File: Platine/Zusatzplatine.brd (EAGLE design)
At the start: 70 x 62.2 mm, 23 parts

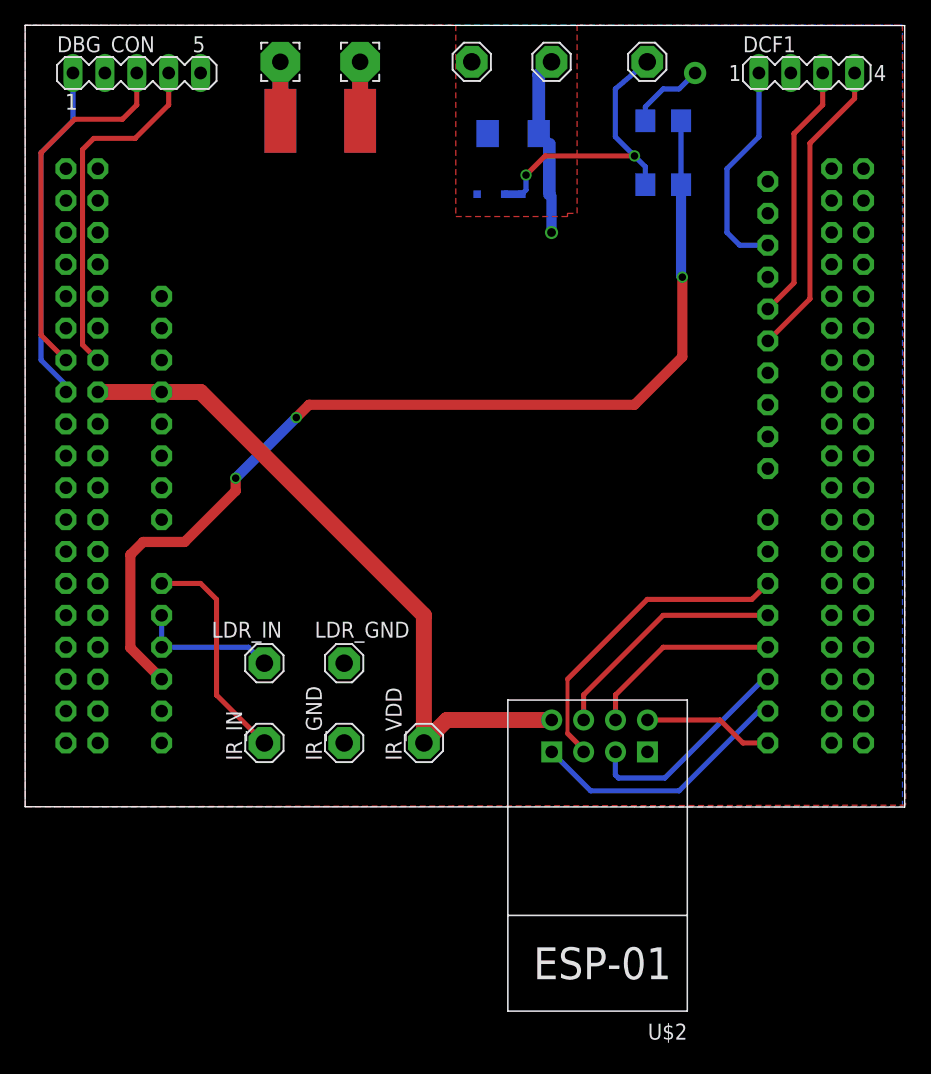
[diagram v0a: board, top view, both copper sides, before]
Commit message: Added Upside Down Mount Option for WiFI Improved Documentation on Board
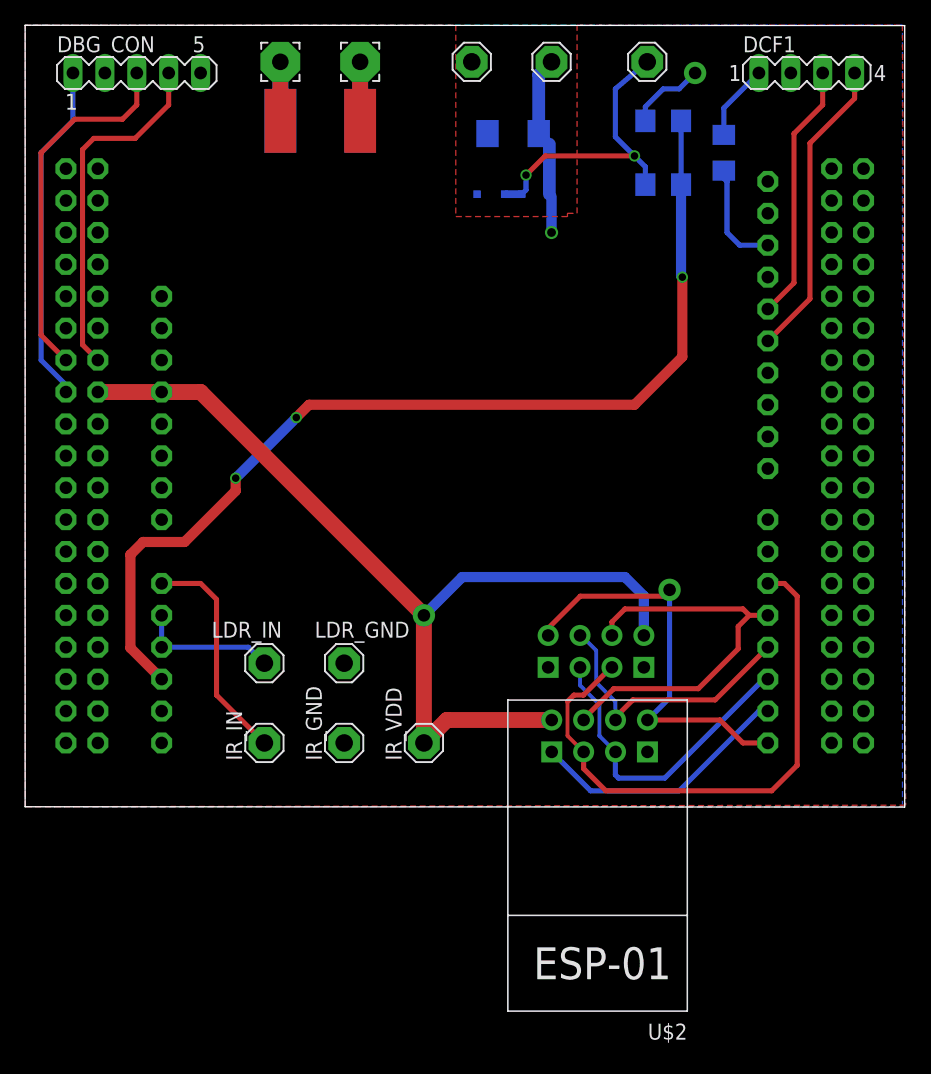
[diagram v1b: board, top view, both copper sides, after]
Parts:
- added R3: 120R, rcl:R1206
- added U$3: ESP01, esp8266modules:ESP01
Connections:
- new net N$2: DCF1.1, R3.1
- net +3V3: now also U$3.VCC
- net GND: now also U$3.GND
- net N$1: now also R3.2; no longer DCF1.1
- net N$12: now also U$3.GPIO0
- net N$13: now also U$3.RST
- net N$14: now also U$3.CH_PD
- net N$15: now also U$3.TX
- net N$16: now also U$3.RX
- net N$17: now also U$3.GPIO2
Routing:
- net N$15: track 10.3 -> 32.9 mm, vias 0 -> 1
- net +3V3: track 54.4 -> 77.0 mm, vias 0 -> 1
- net N$12: track 25.4 -> 45.3 mm
- net N$13: track 19.3 -> 31.9 mm
- net N$17: track 17.3 -> 25.2 mm
- net N$1: track 17.4 -> 9.72 mm
- net N$14: track 15.7 -> 22.6 mm
- net N$2: track 0.00 -> 6.09 mm
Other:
- board text added: "CLK"
- board text added: "DATA"
- board text added: "GND"
- board text added: "NRST"
- board text added: "PON"
- board text added: "SWDIO"
- board text added: "VCC"
- board text added: "WiFi BOT MNT"
- board text added: "WiFi TOP MNT"

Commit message: - DCF-Leitungen umgelegt - Doku korrigiert
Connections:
- net DCF1_DATA: now also U$1.SCL; no longer U$1.D13
- net DCF1_PON: now also U$1.SDA; no longer U$1.D12
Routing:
- net N$16: track 21.1 -> 32.4 mm
- net DCF1_PON: track 24.2 -> 14.0 mm
- net DCF1_DATA: track 20.6 -> 10.4 mm
- net N$14: vias 0 -> 1
- net N$13: vias 0 -> 2
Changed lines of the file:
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@@
 <?xml version="1.0" encoding="utf-8"?>
 <!DOCTYPE eagle SYSTEM "eagle.dtd">
-<eagle version="7.2.0">
+<eagle version="7.4.0">
 <drawing>
 <settings>
@@
 <wire x1="70.028" y1="62.19579375" x2="0" y2="62.22" width="0" layer="20"/>
 <wire x1="0" y1="62.22" x2="0" y2="0" width="0" layer="20"/>
-<text x="19.05" y="33.02" size="1.778" layer="51">WC-WS-Shield for Nucleo
+<text x="19.05" y="33.02" size="1.778" layer="25">WC-WS-Shield for Nucleo
 (c) 2015 K. Neumann, J. Berg</text>
 <text x="33.528" y="53.721" size="1.27" layer="51" rot="R90">LED GND</text>
@@
 <text x="64.008" y="52.832" size="1.016" layer="51" rot="R90">DATA</text>
 <text x="62.992" y="52.705" size="1.016" layer="52" rot="MR90">DATA</text>
-<text x="52.324" y="33.274" size="1.778" layer="52" rot="MR0">WC-WS-Shield for Nucleo
+<text x="52.324" y="33.274" size="1.778" layer="26" rot="MR0">WC-WS-Shield for Nucleo
 (c) 2015 K. Neumann, J. Berg</text>
 </plain>
@@
 <wire x1="44.465" y1="7" x2="46.863" y2="9.398" width="0.4064" layer="1"/>
 <wire x1="46.863" y1="9.398" x2="53.594" y2="9.398" width="0.4064" layer="1"/>
-<wire x1="53.594" y1="9.398" x2="56.769" y2="12.573" width="0.4064" layer="1"/>
-<wire x1="56.769" y1="12.573" x2="56.769" y2="14.351" width="0.4064" layer="1"/>
+<wire x1="53.594" y1="9.398" x2="56.769" y2="12.573" width="0.4064" layer="16"/>
+<wire x1="56.769" y1="12.573" x2="56.769" y2="14.351" width="0.4064" layer="16"/>
 <wire x1="56.769" y1="14.351" x2="57.658" y2="15.24" width="0.4064" layer="1"/>
 <wire x1="57.658" y1="15.24" x2="59.13" y2="15.24" width="0.4064" layer="1"/>
@@
 <wire x1="47.752" y1="15.748" x2="57.15" y2="15.748" width="0.4064" layer="1"/>
 <wire x1="57.15" y1="15.748" x2="57.658" y2="15.24" width="0.4064" layer="1"/>
+<via x="53.594" y="9.398" extent="1-16" drill="0.6" shape="square"/>
+<via x="56.769" y="14.351" extent="1-16" drill="0.6" shape="square"/>
 </signal>
 <signal name="N$14">
@@
 <wire x1="47.005" y1="7.127" x2="48.387" y2="8.509" width="0.4064" layer="1"/>
 <wire x1="48.387" y1="8.509" x2="54.939" y2="8.509" width="0.4064" layer="1"/>
-<wire x1="54.939" y1="8.509" x2="59.13" y2="12.7" width="0.4064" layer="1"/>
+<wire x1="54.939" y1="8.509" x2="59.13" y2="12.7" width="0.4064" layer="16"/>
 <wire x1="44.181" y1="13.6385" x2="44.2735" y2="13.6385" width="0.3048" layer="16"/>
 <wire x1="44.2735" y1="13.6385" x2="45.466" y2="12.446" width="0.3048" layer="16"/>
@@
 <wire x1="46.99" y1="8.382" x2="46.99" y2="6.9225" width="0.3048" layer="16"/>
 <wire x1="46.99" y1="6.9225" x2="47.005" y2="6.9075" width="0.3048" layer="16"/>
+<via x="54.939" y="8.509" extent="1-16" drill="0.6" shape="square"/>
 </signal>
 <signal name="N$15">
@@
 <wire x1="45.0225" y1="1.27" x2="41.925" y2="4.3675" width="0.4064" layer="16"/>
 <contactref element="U$3" pad="RX"/>
-<wire x1="58.42" y1="7.62" x2="49.261" y2="11.0985" width="0" layer="19" extent="16-16"/>
+<wire x1="49.261" y1="11.0985" x2="55.6515" y2="11.0985" width="0.4064" layer="1"/>
+<wire x1="55.6515" y1="11.0985" x2="59.13" y2="7.62" width="0.4064" layer="1"/>
 </signal>
 <signal name="N$17">
@@
 <wire x1="66.04" y1="58.42" x2="66.04" y2="56.388" width="0.4064" layer="1"/>
 <wire x1="66.04" y1="56.388" x2="62.484" y2="52.832" width="0.4064" layer="1"/>
-<contactref element="U$1" pad="D12"/>
-<wire x1="62.484" y1="52.832" x2="62.484" y2="40.438" width="0.4064" layer="1"/>
-<wire x1="62.484" y1="40.438" x2="59.13" y2="37.084" width="0.4064" layer="1"/>
+<contactref element="U$1" pad="SDA"/>
+<wire x1="62.484" y1="52.832" x2="62.484" y2="50.598" width="0.4064" layer="1"/>
+<wire x1="62.484" y1="50.598" x2="59.13" y2="47.244" width="0.4064" layer="1"/>
 </signal>
 <signal name="DCF1_DATA">
 <contactref element="DCF1" pad="3"/>
 <wire x1="63.5" y1="55.88" x2="63.5" y2="58.42" width="0.4064" layer="1"/>
-<wire x1="61.214" y1="41.708" x2="61.214" y2="53.594" width="0.4064" layer="1"/>
 <wire x1="61.214" y1="53.594" x2="63.5" y2="55.88" width="0.4064" layer="1"/>
-<contactref element="U$1" pad="D13"/>
-<wire x1="61.214" y1="41.708" x2="59.13" y2="39.624" width="0.4064" layer="1"/>
+<contactref element="U$1" pad="SCL"/>
+<wire x1="61.214" y1="53.594" x2="61.214" y2="51.868" width="0.4064" layer="1"/>
+<wire x1="61.214" y1="51.868" x2="59.13" y2="49.784" width="0.4064" layer="1"/>
 </signal>
 <signal name="N$1">

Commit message: - Parallele Verbindung zu Morpho-Connectors
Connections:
- removed net AVDD: U$1.AVDD
- net DCF1_DATA: now also U$1.PB8
- net DCF1_PON: now also U$1.PB9
- net IR_IN: now also U$1.PA0
- net LDR_IN: now also U$1.PA1, U$1.PA4
- net LED-OUT: now also U$1.PB0
- net N$1: now also U$1.AVDD
- net N$12: now also U$1.PB4
- net N$13: now also U$1.PB5
- net N$14: now also U$1.PB3
- net N$15: now also U$1.PA3
- net N$16: now also U$1.PA2
- net N$17: now also U$1.PA10
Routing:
- net LDR_IN: track 11.2 -> 18.9 mm
- net N$1: track 9.72 -> 15.4 mm
- net DCF1_PON: track 14.0 -> 19.7 mm
- net DCF1_DATA: track 10.4 -> 16.2 mm
- net IR_IN: track 17.9 -> 23.0 mm
- net N$17: track 25.2 -> 30.3 mm
- net N$16: track 32.4 -> 37.5 mm
- net N$15: track 32.9 -> 38.0 mm
- net N$14: track 22.6 -> 27.7 mm
- net N$13: track 31.9 -> 36.9 mm
- net N$12: track 45.3 -> 50.4 mm
- net LED-OUT: track 80.8 -> 84.5 mm
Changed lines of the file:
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@@
 <wire x1="52.324" y1="42.164" x2="52.222" y2="42.266" width="0.8128" layer="16"/>
 <wire x1="52.222" y1="42.266" x2="52.222" y2="49.53" width="0.8128" layer="16"/>
+<contactref element="U$1" pad="PB0"/>
+<wire x1="8.382" y1="12.648" x2="8.278" y2="12.648" width="0.8128" layer="1"/>
+<wire x1="8.278" y1="12.648" x2="5.79" y2="10.16" width="0.8128" layer="1"/>
 </signal>
 <signal name="+5V">
@@
 <wire x1="17.78" y1="12.7" x2="19.05" y2="11.43" width="0.4064" layer="16"/>
 <wire x1="10.87" y1="12.7" x2="10.87" y2="15.24" width="0.4064" layer="16"/>
-</signal>
-<signal name="AVDD">
-<contactref element="U$1" pad="AVDD"/>
+<contactref element="U$1" pad="PA1"/>
+<contactref element="U$1" pad="PA4"/>
+<wire x1="10.87" y1="15.24" x2="5.79" y2="15.24" width="0.4064" layer="16"/>
+<wire x1="5.79" y1="15.24" x2="5.79" y2="12.7" width="0.4064" layer="16"/>
 </signal>
 <signal name="SWCLK">
@@
 <wire x1="43.18" y1="8.382" x2="43.18" y2="5.6525" width="0.3048" layer="1"/>
 <wire x1="43.18" y1="5.6525" x2="44.465" y2="4.3675" width="0.3048" layer="1"/>
+<contactref element="U$1" pad="PB4"/>
+<wire x1="64.21" y1="17.78" x2="59.13" y2="17.78" width="0.4064" layer="16"/>
 </signal>
 <signal name="N$13">
@@
 <via x="53.594" y="9.398" extent="1-16" drill="0.6" shape="square"/>
 <via x="56.769" y="14.351" extent="1-16" drill="0.6" shape="square"/>
+<contactref element="U$1" pad="PB5"/>
+<wire x1="64.21" y1="15.24" x2="59.13" y2="15.24" width="0.4064" layer="16"/>
 </signal>
 <signal name="N$14">
@@
 <wire x1="46.99" y1="6.9225" x2="47.005" y2="6.9075" width="0.3048" layer="16"/>
 <via x="54.939" y="8.509" extent="1-16" drill="0.6" shape="square"/>
+<contactref element="U$1" pad="PB3"/>
+<wire x1="64.21" y1="12.7" x2="59.13" y2="12.7" width="0.4064" layer="16"/>
 </signal>
 <signal name="N$15">
@@
 <wire x1="51.308" y1="17.272" x2="51.308" y2="8.6705" width="0.4064" layer="16"/>
 <wire x1="51.308" y1="8.6705" x2="49.545" y2="6.9075" width="0.4064" layer="16"/>
+<contactref element="U$1" pad="PA3"/>
+<wire x1="64.21" y1="5.08" x2="59.13" y2="5.08" width="0.4064" layer="16"/>
 </signal>
 <signal name="N$16">
@@
 <wire x1="49.261" y1="11.0985" x2="55.6515" y2="11.0985" width="0.4064" layer="1"/>
 <wire x1="55.6515" y1="11.0985" x2="59.13" y2="7.62" width="0.4064" layer="1"/>
+<contactref element="U$1" pad="PA2"/>
+<wire x1="64.21" y1="7.62" x2="59.13" y2="7.62" width="0.4064" layer="16"/>
 </signal>
 <signal name="N$17">
@@
 <wire x1="45.72" y1="8.128" x2="45.72" y2="5.6525" width="0.3048" layer="16"/>
 <wire x1="45.72" y1="5.6525" x2="47.005" y2="4.3675" width="0.3048" layer="16"/>
+<contactref element="U$1" pad="PA10"/>
+<wire x1="64.21" y1="10.16" x2="59.13" y2="10.16" width="0.4064" layer="16"/>
 </signal>
 <signal name="DCF1_PON">
@@
 <wire x1="62.484" y1="52.832" x2="62.484" y2="50.598" width="0.4064" layer="1"/>
 <wire x1="62.484" y1="50.598" x2="59.13" y2="47.244" width="0.4064" layer="1"/>
+<contactref element="U$1" pad="PB9"/>
+<wire x1="64.21" y1="45.72" x2="60.654" y2="45.72" width="0.4064" layer="16"/>
+<wire x1="60.654" y1="45.72" x2="59.13" y2="47.244" width="0.4064" layer="16"/>
 </signal>
 <signal name="DCF1_DATA">
@@
 <wire x1="61.214" y1="53.594" x2="61.214" y2="51.868" width="0.4064" layer="1"/>
 <wire x1="61.214" y1="51.868" x2="59.13" y2="49.784" width="0.4064" layer="1"/>
+<contactref element="U$1" pad="PB8"/>
+<wire x1="64.21" y1="48.26" x2="60.654" y2="48.26" width="0.4064" layer="16"/>
+<wire x1="60.654" y1="48.26" x2="59.13" y2="49.784" width="0.4064" layer="16"/>
 </signal>
 <signal name="N$1">
@@
 <wire x1="55.626" y1="50.648" x2="55.626" y2="50.038" width="0.4064" layer="16"/>
 <wire x1="55.626" y1="50.038" x2="55.88" y2="49.784" width="0.4064" layer="16"/>
+<contactref element="U$1" pad="AVDD"/>
+<wire x1="64.21" y1="43.18" x2="60.654" y2="43.18" width="0.4064" layer="16"/>
+<wire x1="60.654" y1="43.18" x2="59.13" y2="44.704" width="0.4064" layer="16"/>
 </signal>
 <signal name="+3V3">
@@
 <wire x1="15.24" y1="16.51" x2="15.24" y2="8.89" width="0.4064" layer="1"/>
 <wire x1="15.24" y1="8.89" x2="19.05" y2="5.08" width="0.4064" layer="1"/>
+<contactref element="U$1" pad="PA0"/>
+<wire x1="10.87" y1="17.78" x2="5.79" y2="17.78" width="0.4064" layer="16"/>
 </signal>
 <signal name="N$2">
